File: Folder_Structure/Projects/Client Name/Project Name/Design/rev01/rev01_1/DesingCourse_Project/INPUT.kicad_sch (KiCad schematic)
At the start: 6 parts, among them J8 XT60PW-M

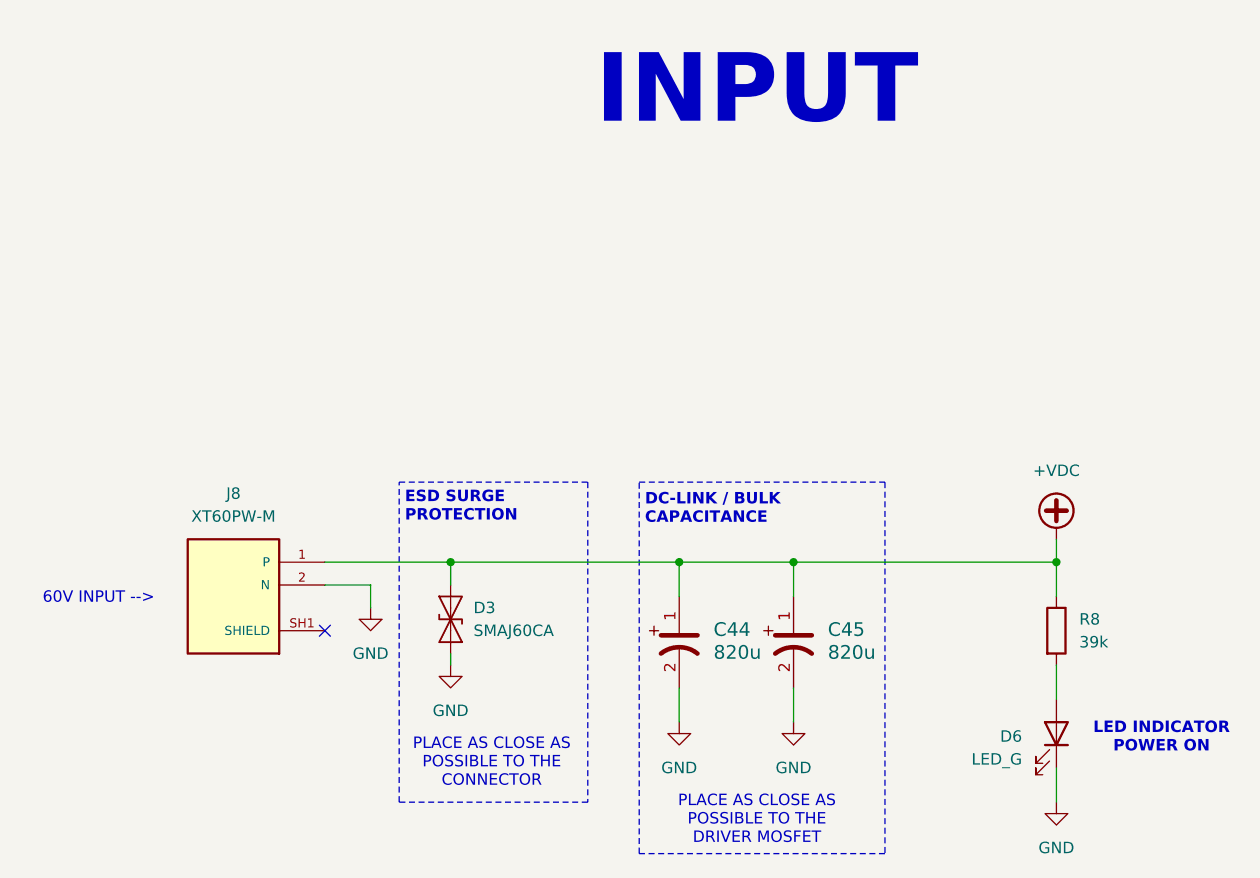
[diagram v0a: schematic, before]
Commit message: Update 12
Until STEP-DOWN page, all components have complete libraries.

Creation and incluison of all logos and labels libraries
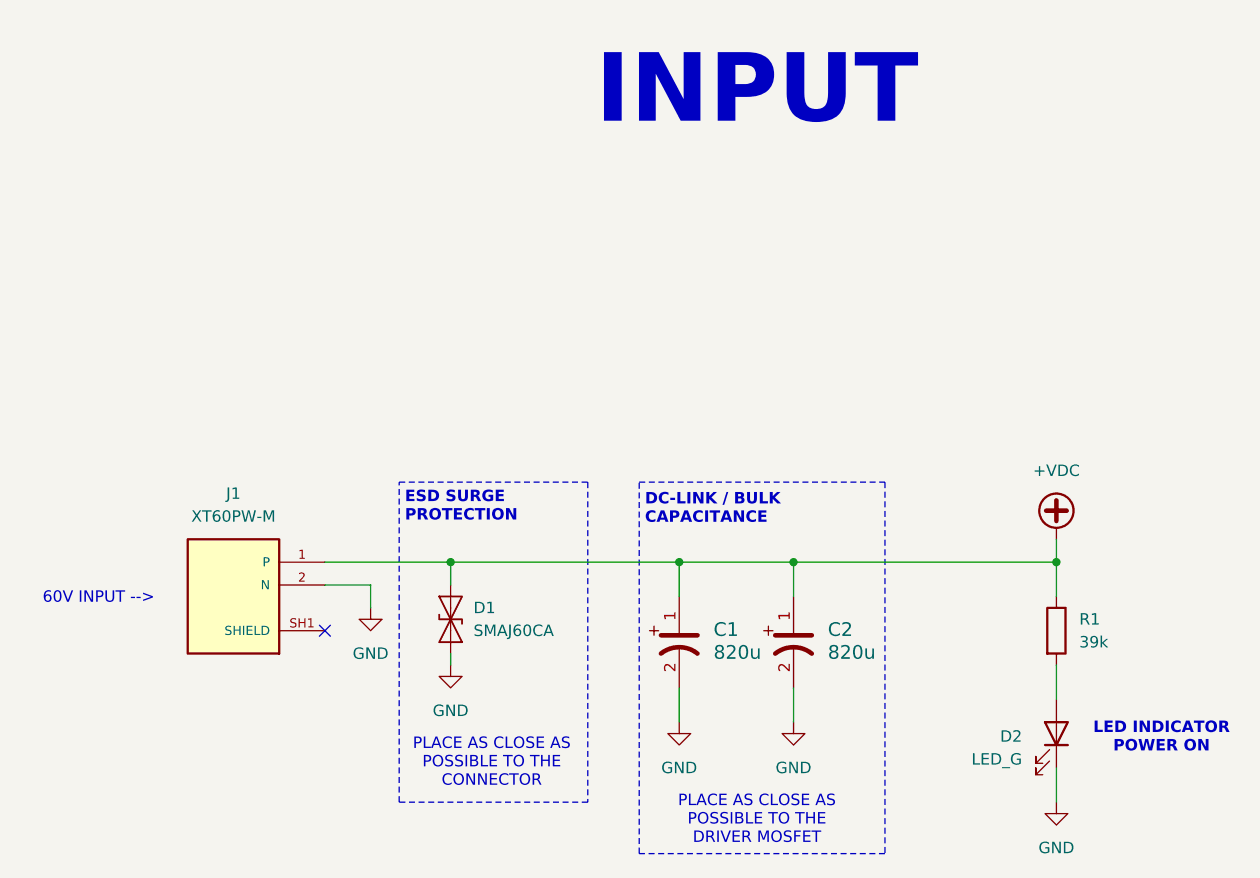
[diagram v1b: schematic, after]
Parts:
- D1: renamed from D3; MNP (none) -> SMAJ60CA; Manufacturer (none) -> Littelfuse; Package (none) -> DO-214AC
- D2: renamed from D6; footprint (none) -> Diode_SMD:D_1206_3216Metric; MPN (none) -> 15-21/GHC-XS1T1/2T; Manufacturer (none) -> Everlight; Package (none) -> 1206
- R1: renamed from R8; footprint (none) -> Resistor_SMD:R_0603_1608Metric; Package (none) -> 0603; Power Rating (none) -> 1/10W; Tolerance (none) -> 1%
- renumbered C44 to C1, C45 to C2, J8 to J1
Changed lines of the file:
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@@
 		(rev "01_1")
 		(company "Integro Consulting AB")
-		(comment 1 "TBD")
+		(comment 1 "00000001")
 		(comment 2 "TBD")
 		(comment 3 "TBD")
@@
 		(dnp no)
 		(fields_autoplaced yes)
-		(property "Reference" "R8"
+		(property "Reference" "R1"
 			(at 195.58 78.7399 0)
 			(effects
@@
 			)
 		)
-		(property "Footprint" ""
+		(property "Footprint" "Resistor_SMD:R_0603_1608Metric"
 			(at 191.262 80.01 90)
 			(effects
@@
 			)
 		)
-		(property "Description" "Resistor"
+		(property "Description" "RES 39k OHM 0603 ±1% 1/10W"
+			(at 193.04 80.01 0)
+			(effects
+				(font
+					(size 1.27 1.27)
+				)
+				(hide yes)
+			)
+		)
+		(property "Package" "0603"
+			(at 193.04 80.01 0)
+			(effects
+				(font
+					(size 1.27 1.27)
+				)
+				(hide yes)
+			)
+		)
+		(property "Tolerance" "1%"
+			(at 193.04 80.01 0)
+			(effects
+				(font
+					(size 1.27 1.27)
+				)
+				(hide yes)
+			)
+		)
+		(property "MPN" ""
+			(at 193.04 80.01 0)
+			(effects
+				(font
+					(size 1.27 1.27)
+				)
+				(hide yes)
+			)
+		)
+		(property "Manufacturer" ""
+			(at 193.04 80.01 0)
+			(effects
+				(font
+					(size 1.27 1.27)
+				)
+				(hide yes)
+			)
+		)
+		(property "Power Rating" "1/10W"
 			(at 193.04 80.01 0)
 			(effects
@@
 			(project ""
 				(path "/e63e39d7-6ac0-4ffd-8aa3-1841a4541b55/b071a88d-8f86-4cf2-bb66-295bf7cf91cc"
-					(reference "R8")
+					(reference "R1")
 					(unit 1)
 				)
@@
 		(dnp no)
 		(fields_autoplaced yes)
-		(property "Reference" "#PWR062"
+		(property "Reference" "#PWR01"
 			(at 116.84 83.82 0)
 			(effects
@@
 			(project "DesingCourse_Project"
 				(path "/e63e39d7-6ac0-4ffd-8aa3-1841a4541b55/b071a88d-8f86-4cf2-bb66-295bf7cf91cc"
-					(reference "#PWR062")
+					(reference "#PWR01")
 					(unit 1)
 				)
@@
 		(dnp no)
 		(fields_autoplaced yes)
-		(property "Reference" "#PWR061"
+		(property "Reference" "#PWR04"
 			(at 163.83 96.52 0)
 			(effects
@@
 			(project "DesingCourse_Project"
 				(path "/e63e39d7-6ac0-4ffd-8aa3-1841a4541b55/b071a88d-8f86-4cf2-bb66-295bf7cf91cc"
-					(reference "#PWR061")
+					(reference "#PWR04")
 					(unit 1)
 				)
@@
 		(dnp no)
 		(fields_autoplaced yes)
-		(property "Reference" "#PWR024"
+		(property "Reference" "#PWR02"
 			(at 125.73 90.17 0)
 			(effects
@@
 			(project "DesingCourse_Project"
 				(path "/e63e39d7-6ac0-4ffd-8aa3-1841a4541b55/b071a88d-8f86-4cf2-bb66-295bf7cf91cc"
-					(reference "#PWR024")
+					(reference "#PWR02")
 					(unit 1)
 				)
@@
 		(dnp no)
 		(fields_autoplaced yes)
-		(property "Reference" "C45"
+		(property "Reference" "C2"
 			(at 167.64 79.8829 0)
 			(effects
@@
 			(project ""
 				(path "/e63e39d7-6ac0-4ffd-8aa3-1841a4541b55/b071a88d-8f86-4cf2-bb66-295bf7cf91cc"
-					(reference "C45")
+					(reference "C2")
 					(unit 1)
 				)
@@
 		(dnp no)
 		(fields_autoplaced yes)
-		(property "Reference" "J8"
+		(property "Reference" "J1"
 			(at 101.6 64.77 0)
 			(effects
@@
 			(project "DesingCourse_Project"
 				(path "/e63e39d7-6ac0-4ffd-8aa3-1841a4541b55/b071a88d-8f86-4cf2-bb66-295bf7cf91cc"
-					(reference "J8")
+					(reference "J1")
 					(unit 1)
 				)
@@
 		(dnp no)
 		(fields_autoplaced yes)
-		(property "Reference" "C44"
+		(property "Reference" "C1"
 			(at 154.94 79.8829 0)
 			(effects
@@
 			(project ""
 				(path "/e63e39d7-6ac0-4ffd-8aa3-1841a4541b55/b071a88d-8f86-4cf2-bb66-295bf7cf91cc"
-					(reference "C44")
+					(reference "C1")
 					(unit 1)
 				)
@@
 		(dnp no)
 		(fields_autoplaced yes)
-		(property "Reference" "D3"
+		(property "Reference" "D1"
 			(at 128.27 77.4699 90)
 			(effects
@@
 		(property "Description" "400W bidirectional Transient Voltage Suppressor, 60.0Vr, SMA(DO-214AC)"
 			(at 125.73 78.74 0)
+			(effects
+				(font
+					(size 1.27 1.27)
+				)
+				(hide yes)
+			)
+		)
+		(property "Package" "DO-214AC"
+			(at 125.73 78.74 90)
+			(effects
+				(font
+					(size 1.27 1.27)
+				)
+				(hide yes)
+			)
+		)
+		(property "MNP" "SMAJ60CA"
+			(at 125.73 78.74 90)
+			(effects
+				(font
+					(size 1.27 1.27)
+				)
+				(hide yes)
+			)
+		)
+		(property "Manufacturer" "Littelfuse"
+			(at 125.73 78.74 90)
 			(effects
 				(font
@@
 			(project ""
 				(path "/e63e39d7-6ac0-4ffd-8aa3-1841a4541b55/b071a88d-8f86-4cf2-bb66-295bf7cf91cc"
-					(reference "D3")
+					(reference "D1")
 					(unit 1)
 				)
@@
 		(dnp no)
 		(fields_autoplaced yes)
-		(property "Reference" "#PWR063"
+		(property "Reference" "#PWR05"
 			(at 193.04 72.39 0)
 			(effects
@@
 			(project "DesingCourse_Project"
 				(path "/e63e39d7-6ac0-4ffd-8aa3-1841a4541b55/b071a88d-8f86-4cf2-bb66-295bf7cf91cc"
-					(reference "#PWR063")
+					(reference "#PWR05")
 					(unit 1)
 				)
@@
 		(dnp no)
 		(fields_autoplaced yes)
-		(property "Reference" "D6"
+		(property "Reference" "D2"
 			(at 189.23 91.7574 90)
 			(effects
@@
 			)
 		)
-		(property "Footprint" ""
+		(property "Footprint" "Diode_SMD:D_1206_3216Metric"
 			(at 193.04 91.44 0)
 			(effects
@@
 			)
 		)
-		(property "Description" "Light emitting diode"
+		(property "Description" "LED GREEN CLEAR 1206 SMD"
 			(at 193.04 91.44 0)
 			(effects
@@
 		(property "Sim.Pins" "1=K 2=A"
 			(at 193.04 91.44 0)
+			(effects
+				(font
+					(size 1.27 1.27)
+				)
+				(hide yes)
+			)
+		)
+		(property "Manufacturer" "Everlight"
+			(at 193.04 91.44 90)
+			(effects
+				(font
+					(size 1.27 1.27)
+				)
+				(hide yes)
+			)
+		)
+		(property "MPN" "15-21/GHC-XS1T1/2T"
+			(at 193.04 91.44 90)
+			(effects
+				(font
+					(size 1.27 1.27)
+				)
+				(hide yes)
+			)
+		)
+		(property "Package" "1206"
+			(at 193.04 91.44 90)
 			(effects
 				(font
@@
 			(project "DesingCourse_Project"
 				(path "/e63e39d7-6ac0-4ffd-8aa3-1841a4541b55/b071a88d-8f86-4cf2-bb66-295bf7cf91cc"
-					(reference "D6")
+					(reference "D2")
 					(unit 1)
 				)
@@
 		(dnp no)
 		(fields_autoplaced yes)
-		(property "Reference" "#PWR064"
+		(property "Reference" "#PWR06"
 			(at 193.04 105.41 0)
 			(effects
@@
 			(project "DesingCourse_Project"
 				(path "/e63e39d7-6ac0-4ffd-8aa3-1841a4541b55/b071a88d-8f86-4cf2-bb66-295bf7cf91cc"
-					(reference "#PWR064")
+					(reference "#PWR06")
 					(unit 1)
 				)
@@
 		(dnp no)
 		(fields_autoplaced yes)
-		(property "Reference" "#PWR060"
+		(property "Reference" "#PWR03"
 			(at 151.13 96.52 0)
 			(effects
@@
 			(project "DesingCourse_Project"
 				(path "/e63e39d7-6ac0-4ffd-8aa3-1841a4541b55/b071a88d-8f86-4cf2-bb66-295bf7cf91cc"
-					(reference "#PWR060")
+					(reference "#PWR03")
 					(unit 1)
 				)

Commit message: Update 16
Initial component placement done
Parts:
- D1: MNP SMAJ60CA -> (none); MPN (none) -> SMAJ60CA
- J1: MF AMASS -> (none)
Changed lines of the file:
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@@
+			)
+		)
+		(property "MNP" ""
+			(at 193.04 80.01 0)
+			(effects
+				(font
+					(size 1.27 1.27)
+				)
+				(hide yes)
+			)
+		)
+		(property "MF" ""
+			(at 193.04 80.01 0)
+			(effects
+				(font
+					(size 1.27 1.27)
+				)
+				(hide yes)
 			)
 		)
@@
 			)
 		)
+		(property "MNP" ""
+			(at 163.83 81.28 0)
+			(effects
+				(font
+					(size 1.27 1.27)
+				)
+				(hide yes)
+			)
+		)
+		(property "MF" ""
+			(at 163.83 81.28 0)
+			(effects
+				(font
+					(size 1.27 1.27)
+				)
+				(hide yes)
+			)
+		)
 		(pin "1"
 		)
@@
 			)
 		)
-		(property "MF" "AMASS"
-			(at 101.6 74.93 0)
-			(effects
-				(font
-					(size 1.27 1.27)
-				)
-				(justify bottom)
-				(hide yes)
-			)
-		)
 		(property "MAXIMUM_PACKAGE_HEIGHT" "8.4 mm"
 			(at 101.6 74.93 0)
@@
 			)
 		)
+		(property "MF" ""
+			(at 101.6 74.93 0)
+			(effects
+				(font
+					(size 1.27 1.27)
+				)
+				(hide yes)
+			)
+		)
+		(pin "SH2"
+		)
 		(pin "SH1"
 		)
 		(pin "1"
 		)
-		(pin "SH2"
-		)
 		(pin "2"
 		)
 		(instances
-			(project "DesingCourse_Project"
+			(project ""
 				(path "/e63e39d7-6ac0-4ffd-8aa3-1841a4541b55/b071a88d-8f86-4cf2-bb66-295bf7cf91cc"
 					(reference "J1")
@@
 			)
 		)
+		(property "MNP" ""
+			(at 151.13 81.28 0)
+			(effects
+				(font
+					(size 1.27 1.27)
+				)
+				(hide yes)
+			)
+		)
+		(property "MF" ""
+			(at 151.13 81.28 0)
+			(effects
+				(font
+					(size 1.27 1.27)
+				)
+				(hide yes)
+			)
+		)
 		(pin "1"
 		)
@@
 			)
 		)
-		(property "MNP" "SMAJ60CA"
+		(property "MPN" "SMAJ60CA"
 			(at 125.73 78.74 90)
 			(effects
@@
 		)
 		(property "Manufacturer" "Littelfuse"
+			(at 125.73 78.74 90)
+			(effects
+				(font
+					(size 1.27 1.27)
+				)
+				(hide yes)
+			)
+		)
+		(property "MNP" ""
+			(at 125.73 78.74 90)
+			(effects
+				(font
+					(size 1.27 1.27)
+				)
+				(hide yes)
+			)
+		)
+		(property "MF" ""
 			(at 125.73 78.74 90)
 			(effects
@@
 			(at 193.04 91.44 90)
 			(effects
+				(font
+					(size 1.27 1.27)
+				)
+				(hide yes)
+			)
+		)
+		(property "MNP" ""
+			(at 193.04 91.44 90)
+			(effects
+				(font
+					(size 1.27 1.27)
+				)
+				(hide yes)
+			)
+		)
+		(property "MF" ""
+			(at 193.04 91.44 90)
+			(effects

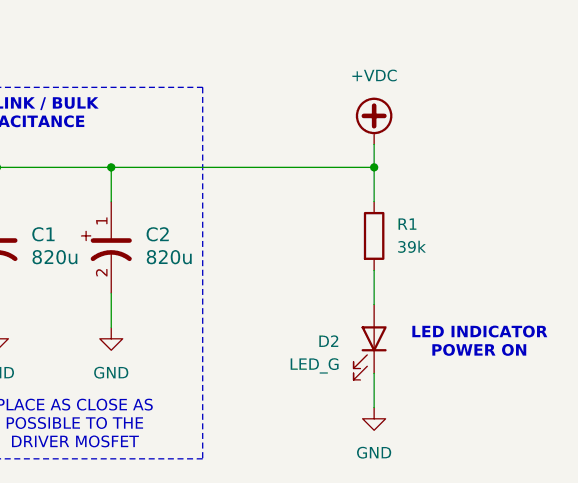
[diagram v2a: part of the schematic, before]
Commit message: Update17
Design rules and stack defined.

Check againg DR and proceed with layout.
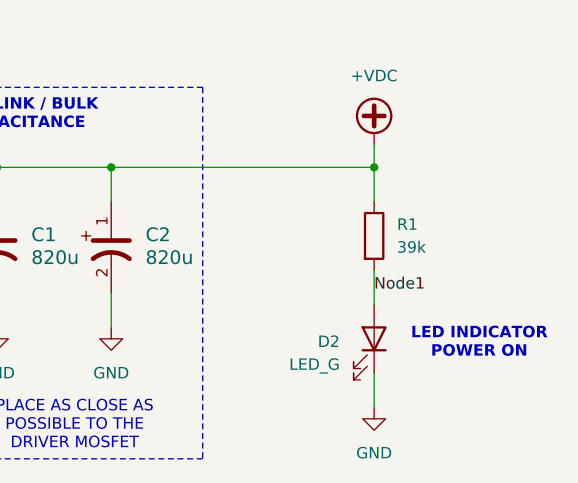
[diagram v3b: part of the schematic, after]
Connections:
- net Node1: now reaches D2.2 (A), R1.2
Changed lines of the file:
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@@
+		)
+	)
+	(label "Node1"
+		(at 193.04 86.36 0)
+		(effects
+			(font
+				(size 1.27 1.27)
+			)
+			(justify left bottom)
 		)
 	)
